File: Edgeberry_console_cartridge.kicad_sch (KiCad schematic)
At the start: 26 parts, among them J1 USB_B, J3 Screw_Terminal_01x03, U1 FT232RL, U2 MCP2515, U3 MCP2562, Y1 16MHz

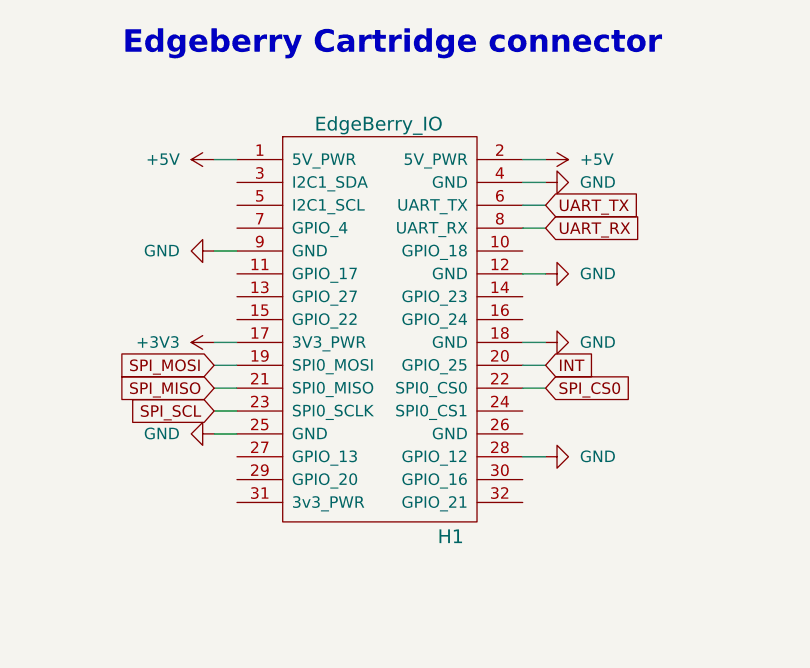
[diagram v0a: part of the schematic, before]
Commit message: Update to KiCad 8 + footprint cleanup
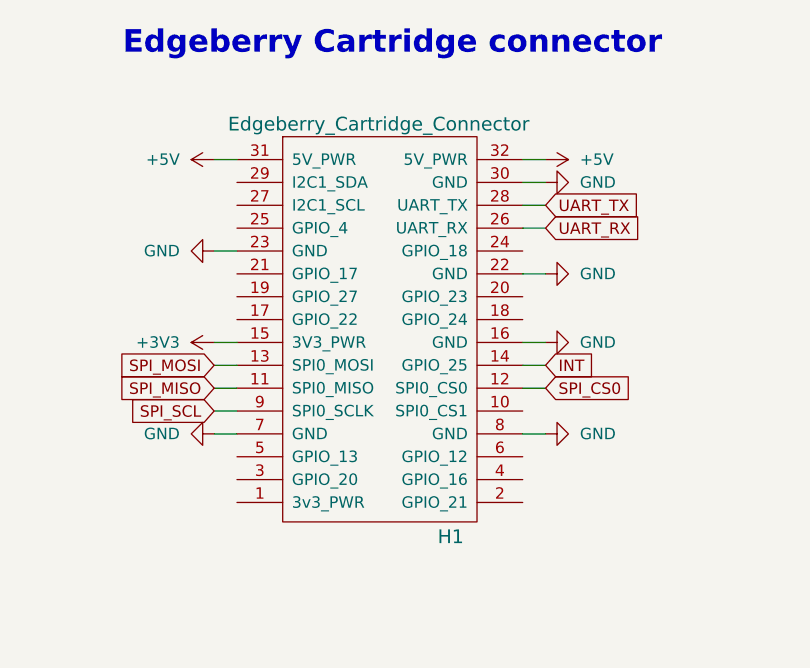
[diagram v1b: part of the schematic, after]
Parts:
- H1: value EdgeBerry_IO -> Edgeberry_Cartridge_Connector; footprint emcosys:EdgeBerry_IO_male -> Connector_PinHeader_2.54mm:PinHeader_2x16_P2.54mm_Horizontal
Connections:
- net +3V3: now also H1.15 (3V3_PWR); no longer H1.17 (3V3_PWR)
- net +5V: now also H1.31 (5V_PWR), H1.32 (5V_PWR); no longer H1.1 (5V_PWR), H1.2 (5V_PWR)
- net GND: now also H1.16 (GND), H1.22 (GND), H1.23 (GND), H1.30 (GND), H1.7 (GND), H1.8 (GND); no longer H1.12 (GND), H1.18 (GND), H1.25 (GND), H1.28 (GPIO_12), H1.4 (GND), H1.9 (GND)
- net INT: now also H1.14 (GPIO_25); no longer H1.20 (GPIO_25)
- net SPI_CS0: now also H1.12 (SPI0_CS0); no longer H1.22 (SPI0_CS0)
- net SPI_MISO: now also H1.11 (SPI0_MISO); no longer H1.21 (SPI0_MISO)
- net SPI_MOSI: now also H1.13 (SPI0_MOSI); no longer H1.19 (SPI0_MOSI)
- net SPI_SCL: now also H1.9 (SPI0_SCLK); no longer H1.23 (SPI0_SCLK)
- net UART_RX: now also H1.26 (UART_RX); no longer H1.8 (UART_RX)
- net UART_TX: now also H1.28 (UART_TX); no longer H1.6 (UART_TX)

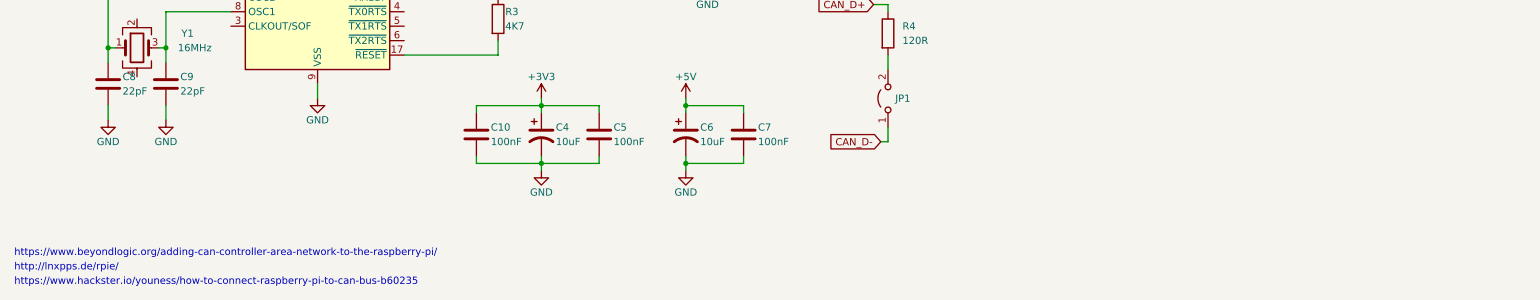
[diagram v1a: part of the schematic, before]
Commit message: Open Source Hardware license: CERN-OHL-W
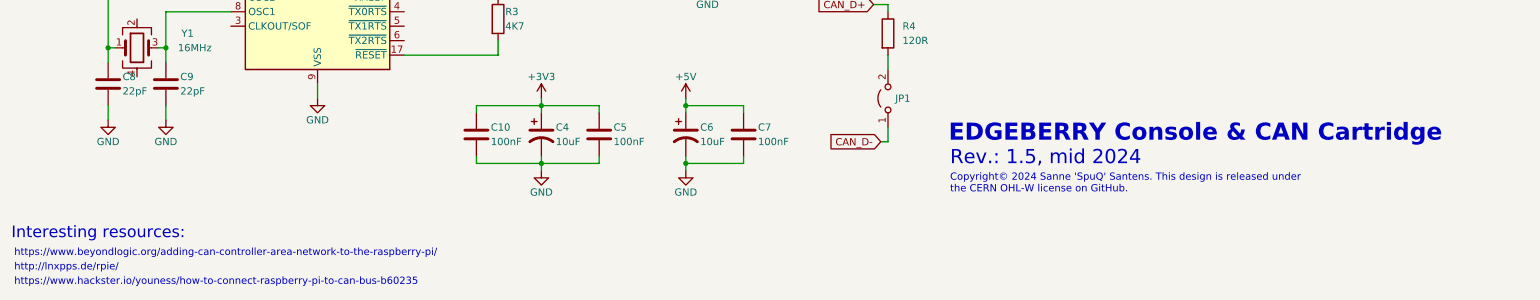
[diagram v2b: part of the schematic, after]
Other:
- note added: "Copyright© 2024 Sanne 'SpuQ' Santens. This design is released under the CERN OHL-W license on GitHub."
- note added: "EDGEBERRY Console & CAN Cartridge"
- note added: "Interesting resources:"
- note added: "Rev.: 1.5, mid 2024"
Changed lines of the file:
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@@
+		)
+	)
+	(text "Interesting resources:"
+		(exclude_from_sim no)
+		(at 13.462 188.722 0)
+		(effects
+			(font
+				(size 2.032 2.032)
+			)
+			(justify left bottom)
 		)
 	)
@@
 		)
 	)
+	(text "EDGEBERRY Console & CAN Cartridge"
+		(exclude_from_sim no)
+		(at 178.308 171.704 0)
+		(effects
+			(font
+				(size 3 3)
+				(thickness 0.4)
+				(bold yes)
+			)
+			(justify left bottom)
+		)
+	)
 	(text "UART to USB"
 		(exclude_from_sim no)
@@
 		)
 	)
+	(text "Rev.: 1.5, mid 2024\n"
+		(exclude_from_sim no)
+		(at 178.562 175.768 0)
+		(effects
+			(font
+				(size 2.4892 2.4892)
+			)
+			(justify left bottom)
+		)
+	)
+	(text "Copyright© 2024 Sanne 'SpuQ' Santens. This design is released under\nthe CERN OHL-W license on GitHub."
+		(exclude_from_sim no)
+		(at 178.562 178.816 0)
+		(effects
+			(font
+				(size 1.27 1.27)
+			)
+			(justify left)
+		)
+	)

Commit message: cleanup
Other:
- note added: "CAN-bus termination resistor"
- note added: "Console & CAN interface, Rev.: 1.5, mid 2024"
- note added: "EDGEBERRY HARDWARE CARTRIDGE"
- note added: "Edgeberry Hardware Cartridge connector"
- note removed: "EDGEBERRY Console & CAN Cartridge"
- note removed: "Edgeberry Cartridge connector"
- note removed: "Interesting resources:"
- note removed: "Rev.: 1.5, mid 2024"
- note removed: "http://lnxpps.de/rpie/"
- note removed: "https://www.beyondlogic.org/adding-can-controller-area-network-to-the-raspberry-pi/"
- note removed: "https://www.hackster.io/youness/how-to-connect-raspberry-pi-to-can-bus-b60235"
- moved on the sheet: H1
